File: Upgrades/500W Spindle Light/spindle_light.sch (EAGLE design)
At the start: 10 parts

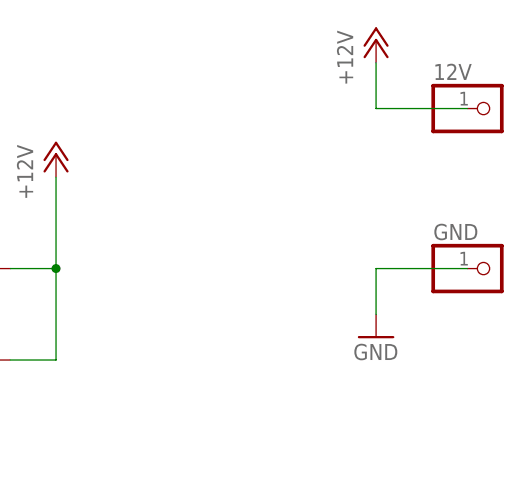
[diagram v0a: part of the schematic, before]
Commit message: Spindle light update
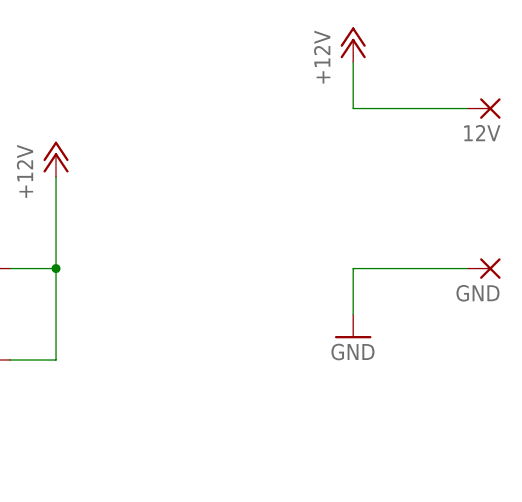
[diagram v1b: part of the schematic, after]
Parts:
- 12V, GND: value (none) -> WIREPAD2,54/1,1; device pinhead:PINHD-1X1 -> wirepad:WIREPAD2,54/1,1
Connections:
- net +12V: now also 12V.P; no longer 12V.1
- net GND: now also GND.P; no longer GND.1
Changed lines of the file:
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@@
 <part name="GND1" library="supply1" library_urn="urn:adsk.eagle:library:371" deviceset="GND" device=""/>
 <part name="FRAME2" library="frames" library_urn="urn:adsk.eagle:library:229" deviceset="A4L-LOC" device=""/>
-<part name="12V" library="pinhead" library_urn="urn:adsk.eagle:library:325" deviceset="PINHD-1X1" device="" package3d_urn="urn:adsk.eagle:package:22485/2"/>
-<part name="GND" library="pinhead" library_urn="urn:adsk.eagle:library:325" deviceset="PINHD-1X1" device="" package3d_urn="urn:adsk.eagle:package:22485/2"/>
 <part name="P+2" library="supply1" library_urn="urn:adsk.eagle:library:371" deviceset="+12V" device=""/>
 <part name="GND2" library="supply1" library_urn="urn:adsk.eagle:library:371" deviceset="GND" device=""/>
+<part name="GND" library="wirepad" library_urn="urn:adsk.eagle:library:412" deviceset="WIREPAD" device="2,54/1,1" package3d_urn="urn:adsk.eagle:package:30836/1"/>
+<part name="12V" library="wirepad" library_urn="urn:adsk.eagle:library:412" deviceset="WIREPAD" device="2,54/1,1" package3d_urn="urn:adsk.eagle:package:30836/1"/>
 </parts>
 <sheets>
@@
 <attribute name="SHEET" x="149.225" y="-63.5" size="2.54" layer="94"/>
 </instance>
-<instance part="12V" gate="G$1" x="127" y="40.64" smashed="yes">
-<attribute name="NAME" x="120.65" y="43.815" size="1.778" layer="95"/>
-<attribute name="VALUE" x="120.65" y="35.56" size="1.778" layer="96"/>
+<instance part="P+2" gate="1" x="111.76" y="48.26" smashed="yes">
+<attribute name="VALUE" x="109.22" y="43.18" size="1.778" layer="96" rot="R90"/>
 </instance>
-<instance part="GND" gate="G$1" x="127" y="22.86" smashed="yes">
-<attribute name="NAME" x="120.65" y="26.035" size="1.778" layer="95"/>
-<attribute name="VALUE" x="120.65" y="17.78" size="1.778" layer="96"/>
+<instance part="GND2" gate="1" x="111.76" y="15.24" smashed="yes">
+<attribute name="VALUE" x="109.22" y="12.7" size="1.778" layer="96"/>
 </instance>
-<instance part="P+2" gate="1" x="114.3" y="48.26" smashed="yes">
-<attribute name="VALUE" x="111.76" y="43.18" size="1.778" layer="96" rot="R90"/>
+<instance part="GND" gate="G$1" x="127" y="22.86" smashed="yes" rot="R180">
+<attribute name="NAME" x="128.143" y="21.0058" size="1.778" layer="95" rot="R180"/>
+<attribute name="VALUE" x="128.143" y="26.162" size="1.778" layer="96" rot="R180" display="off"/>
 </instance>
-<instance part="GND2" gate="1" x="114.3" y="15.24" smashed="yes">
-<attribute name="VALUE" x="111.76" y="12.7" size="1.778" layer="96"/>
+<instance part="12V" gate="G$1" x="127" y="40.64" smashed="yes" rot="R180">
+<attribute name="NAME" x="128.143" y="38.7858" size="1.778" layer="95" rot="R180"/>
+<attribute name="VALUE" x="128.143" y="43.942" size="1.778" layer="96" rot="R180" display="off"/>
 </instance>
 </instances>
@@
 </segment>
 <segment>
-<pinref part="GND" gate="G$1" pin="1"/>
 <pinref part="GND2" gate="1" pin="GND"/>
-<wire x1="124.46" y1="22.86" x2="114.3" y2="22.86" width="0.1524" layer="91"/>
-<wire x1="114.3" y1="22.86" x2="114.3" y2="17.78" width="0.1524" layer="91"/>
+<wire x1="124.46" y1="22.86" x2="111.76" y2="22.86" width="0.1524" layer="91"/>
+<wire x1="111.76" y1="22.86" x2="111.76" y2="17.78" width="0.1524" layer="91"/>
+<pinref part="GND" gate="G$1" pin="P"/>
 </segment>
 </net>
@@
 </segment>
 <segment>
-<pinref part="12V" gate="G$1" pin="1"/>
 <pinref part="P+2" gate="1" pin="+12V"/>
-<wire x1="124.46" y1="40.64" x2="114.3" y2="40.64" width="0.1524" layer="91"/>
-<wire x1="114.3" y1="40.64" x2="114.3" y2="45.72" width="0.1524" layer="91"/>
+<wire x1="124.46" y1="40.64" x2="111.76" y2="40.64" width="0.1524" layer="91"/>
+<wire x1="111.76" y1="40.64" x2="111.76" y2="45.72" width="0.1524" layer="91"/>
+<pinref part="12V" gate="G$1" pin="P"/>
 </segment>
 </net>

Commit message: GND error fix
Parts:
- 12V, GND: value WIREPAD2,54/1,1 -> (none); device wirepad:WIREPAD2,54/1,1 -> wirepad:SMD5
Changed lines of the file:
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@@
 <part name="P+2" library="supply1" library_urn="urn:adsk.eagle:library:371" deviceset="+12V" device=""/>
 <part name="GND2" library="supply1" library_urn="urn:adsk.eagle:library:371" deviceset="GND" device=""/>
-<part name="GND" library="wirepad" library_urn="urn:adsk.eagle:library:412" deviceset="WIREPAD" device="2,54/1,1" package3d_urn="urn:adsk.eagle:package:30836/1"/>
-<part name="12V" library="wirepad" library_urn="urn:adsk.eagle:library:412" deviceset="WIREPAD" device="2,54/1,1" package3d_urn="urn:adsk.eagle:package:30836/1"/>
+<part name="12V" library="wirepad" library_urn="urn:adsk.eagle:library:412" deviceset="SMD5" device="" package3d_urn="urn:adsk.eagle:package:30841/1"/>
+<part name="GND" library="wirepad" library_urn="urn:adsk.eagle:library:412" deviceset="SMD5" device="" package3d_urn="urn:adsk.eagle:package:30841/1"/>
 </parts>
 <sheets>
@@
 <attribute name="VALUE" x="109.22" y="12.7" size="1.778" layer="96"/>
 </instance>
-<instance part="GND" gate="G$1" x="127" y="22.86" smashed="yes" rot="R180">
+<instance part="12V" gate="1" x="127" y="40.64" smashed="yes" rot="R180">
+<attribute name="NAME" x="128.143" y="38.7858" size="1.778" layer="95" rot="R180"/>
+<attribute name="VALUE" x="128.143" y="43.942" size="1.778" layer="96" rot="R180"/>
+</instance>
+<instance part="GND" gate="1" x="127" y="22.86" smashed="yes" rot="R180">
 <attribute name="NAME" x="128.143" y="21.0058" size="1.778" layer="95" rot="R180"/>
-<attribute name="VALUE" x="128.143" y="26.162" size="1.778" layer="96" rot="R180" display="off"/>
-</instance>
-<instance part="12V" gate="G$1" x="127" y="40.64" smashed="yes" rot="R180">
-<attribute name="NAME" x="128.143" y="38.7858" size="1.778" layer="95" rot="R180"/>
-<attribute name="VALUE" x="128.143" y="43.942" size="1.778" layer="96" rot="R180" display="off"/>
+<attribute name="VALUE" x="128.143" y="26.162" size="1.778" layer="96" rot="R180"/>
 </instance>
 </instances>
@@
 <wire x1="124.46" y1="22.86" x2="111.76" y2="22.86" width="0.1524" layer="91"/>
 <wire x1="111.76" y1="22.86" x2="111.76" y2="17.78" width="0.1524" layer="91"/>
-<pinref part="GND" gate="G$1" pin="P"/>
+<pinref part="GND" gate="1" pin="P"/>
 </segment>
 </net>
@@
 <wire x1="124.46" y1="40.64" x2="111.76" y2="40.64" width="0.1524" layer="91"/>
 <wire x1="111.76" y1="40.64" x2="111.76" y2="45.72" width="0.1524" layer="91"/>
-<pinref part="12V" gate="G$1" pin="P"/>
+<pinref part="12V" gate="1" pin="P"/>
 </segment>
 </net>
